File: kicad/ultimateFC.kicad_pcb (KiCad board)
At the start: 8 copper layers, 30.4 x 25.2 mm, 194 parts, among them J1 USB_B_Micro, J2 10132797-011100LF, J3 10132797-011100LF, J4 10132797-011100LF, J5 10132797-011100LF, J6 10132797-011100LF, Q1 DMP2066LSN-7, U1 EFM8BB21F16G-C-QFN20R, U10 NCP81253MNTBG, U11 SiZ200DT, U12 NCP81253MNTBG, U13 SiZ200DT, U14 TPS62824ADMQ, U15 SiZ200DT, U16 NCP81253MNTBG, U17 NCP81253MNTBG, U18 NCP81253MNTBG, U19 NCP81253MNTBG, U2 EFM8BB21F16G-C-QFN20R, U20 SiZ200DT, U21 SiZ200DT, U22 SiZ200DT, U23 SiZ200DT, U24 EFM8BB21F16G-C-QFN20R, U25 NCP81253MNTBG, U26 SiZ200DT, U27 NCP81253MNTBG, U28 NCP81253MNTBG, U29 SiZ200DT, U3 NCP81253MNTBG, U30 SiZ200DT, U31 INA186, U32 LMR33630CQRNX, U33 STM32F745VGHx, U34 AB7456, U35 ZOE-M8Q_ZOE-M8Q, U36 ICM-20602, U37 S25FL064L, U39 BMP280, U4 SiZ200DT, U6 EFM8BB21F16G-C-QFN20R, U7 NCP81253MNTBG, U8 SiZ200DT, U9 NCP81253MNTBG, X1 Molex_734120110, Y1 CSTNE8M00G550000R0, Y2 ECS-270-8-47Q-CES-TR

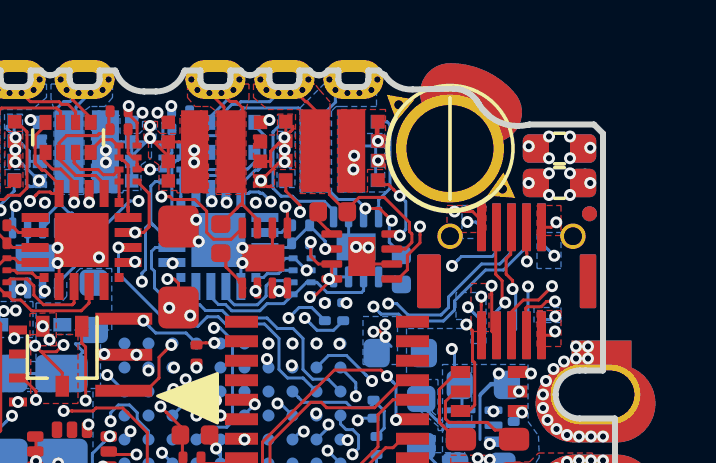
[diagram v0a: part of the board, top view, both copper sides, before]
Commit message: added a few 3d components
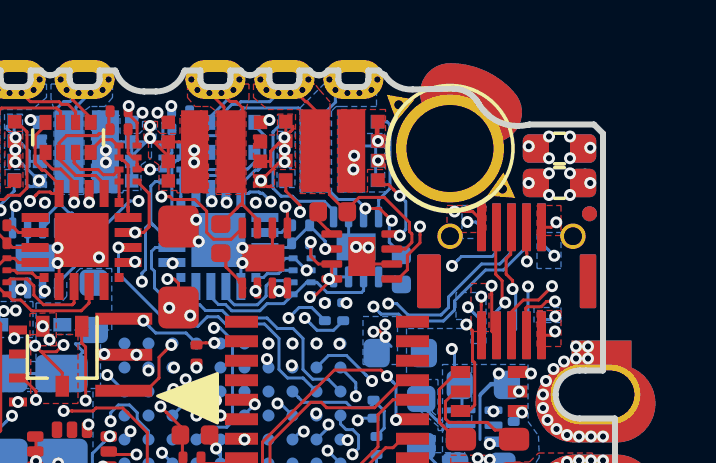
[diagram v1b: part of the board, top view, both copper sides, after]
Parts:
- removed the REF** at (197.1, 64.2) (x2)
- added REF**: Fiducial_0.5mm_Dia_1mm_Outer, Fiducial:Fiducial_0.5mm_Dia_1mm_Outer, F.Cu at (197.1, 64.2)
- added REF**: Fiducial_0.5mm_Dia_1mm_Outer, Fiducial:Fiducial_0.5mm_Dia_1mm_Outer, B.Cu at (197.1, 64.2)
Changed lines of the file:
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@@
   (general
     (thickness 1.2)
-    (drawings 529)
+    (drawings 528)
     (tracks 3920)
     (zones 0)
@@
     (pad 2 smd rect (at 0.6 0.25 90) (size 0.5 0.3) (layers F.Cu F.Paste F.Mask)
       (net 1 GND))
+    (model C:/Users/Christian/Desktop/Elektronik/yolo_fc/yolo-fc/kicad/3D/idc.stp
+      (offset (xyz 0.1 0 0))
+      (scale (xyz 1 1 1))
+      (rotate (xyz -90 0 0))
+    )
   )
   (module ultimateFC:C_AVX_Super_Low_ESL (layer F.Cu)
@@
     (pad 2 smd rect (at 0.6 0.25 90) (size 0.5 0.3) (layers F.Cu F.Paste F.Mask)
       (net 1 GND))
+    (model C:/Users/Christian/Desktop/Elektronik/yolo_fc/yolo-fc/kicad/3D/idc.stp
+      (offset (xyz 0.1 0 0))
+      (scale (xyz 1 1 1))
+      (rotate (xyz -90 0 0))
+    )
   )
   (module ultimateFC:C_AVX_Super_Low_ESL (layer F.Cu)
@@
     (pad 2 smd rect (at 0.6 0.25 90) (size 0.5 0.3) (layers F.Cu F.Paste F.Mask)
       (net 3 +3V3))
+    (model C:/Users/Christian/Desktop/Elektronik/yolo_fc/yolo-fc/kicad/3D/idc.stp
+      (offset (xyz 0.1 0 0))
+      (scale (xyz 1 1 1))
+      (rotate (xyz -90 0 0))
+    )
   )
   (module ultimateFC:C_AVX_Super_Low_ESL (layer B.Cu)
@@
     (pad 2 smd rect (at 0.6 -0.25 270) (size 0.5 0.3) (layers B.Cu B.Paste B.Mask)
       (net 2 +5V))
+    (model C:/Users/Christian/Desktop/Elektronik/yolo_fc/yolo-fc/kicad/3D/idc.stp
+      (offset (xyz 0.1 0 0))
+      (scale (xyz 1 1 1))
+      (rotate (xyz -90 0 0))
+    )
   )
   (module ultimateFC:C_AVX_Super_Low_ESL (layer B.Cu)
@@
     (pad 2 smd rect (at 0.6 -0.25 90) (size 0.5 0.3) (layers B.Cu B.Paste B.Mask)
       (net 1 GND))
+    (model ${KIPRJMOD}/3D/idc.stp
+      (offset (xyz 0.1 0 0))
+      (scale (xyz 1 1 1))
+      (rotate (xyz -90 0 0))
+    )
   )
   (module ultimateFC:C_AVX_Super_Low_ESL (layer F.Cu)
@@
     (pad 2 smd rect (at 0.6 0.25 90) (size 0.5 0.3) (layers F.Cu F.Paste F.Mask)
       (net 1 GND))
+    (model C:/Users/Christian/Desktop/Elektronik/yolo_fc/yolo-fc/kicad/3D/idc.stp
+      (offset (xyz 0.1 0 0))
+      (scale (xyz 1 1 1))
+      (rotate (xyz -90 0 0))
+    )
   )
   (module ultimateFC:C_AVX_Super_Low_ESL (layer B.Cu)
@@
     (pad 2 smd rect (at 0.6 -0.25 90) (size 0.5 0.3) (layers B.Cu B.Paste B.Mask)
       (net 3 +3V3))
+    (model C:/Users/Christian/Desktop/Elektronik/yolo_fc/yolo-fc/kicad/3D/idc.stp
+      (offset (xyz 0.1 0 0))
+      (scale (xyz 1 1 1))
+      (rotate (xyz -90 0 0))
+    )
   )
   (module ultimateFC:C_AVX_Super_Low_ESL (layer B.Cu)
@@
     (pad 2 smd rect (at 0.6 -0.25 270) (size 0.5 0.3) (layers B.Cu B.Paste B.Mask)
       (net 2 +5V))
+    (model C:/Users/Christian/Desktop/Elektronik/yolo_fc/yolo-fc/kicad/3D/idc.stp
+      (offset (xyz 0.1 0 0))
+      (scale (xyz 1 1 1))
+      (rotate (xyz -90 0 0))
+    )
   )
   (module ultimateFC:10132797-011100LF (layer F.Cu)
@@
     (pad 1 smd roundrect (at 1 -1.8 180) (size 0.3 1.6) (layers F.Cu F.Paste F.Mask) (roundrect_rratio 0.1)
       (net 1 GND))
-    (model ${KIPRJMOD}/10132797-011100LF.stp
+    (model ${KIPRJMOD}/3D/10132797-011100LF.stp
       (at (xyz 0 0 0))
       (scale (xyz 1 1 1))
@@
     (pad "" smd roundrect (at 2.75 0 180) (size 0.8 1.8) (layers F.Cu F.Paste F.Mask) (roundrect_rratio 0.1))
     (pad "" smd roundrect (at -2.6 0) (size 0.55 1.8) (layers F.Cu F.Paste F.Mask) (roundrect_rratio 0.1))
-    (model ${KIPRJMOD}/10132797-011100LF.stp
+    (model ${KIPRJMOD}/3D/10132797-011100LF.stp
       (at (xyz 0 0 0))
       (scale (xyz 1 1 1))
@@
     (pad 1 thru_hole circle (at -2.05 -1.5) (size 0.85 0.85) (drill 0.6) (layers *.Cu *.Mask)
       (net 1 GND) (solder_mask_margin -0.05))
-    (model ${KIPRJMOD}/10132797-011100LF.stp
+    (model ${KIPRJMOD}/3D/10132797-011100LF.stp
       (at (xyz 0 0 0))
       (scale (xyz 1 1 1))
@@
   (gr_poly (pts (xy 183.2 67.825) (xy 181.2 67.075) (xy 183.2 66.175)) (layer B.SilkS) (width 0.1))
   (gr_poly (pts (xy 184.75 69.5) (xy 182.75 70.25) (xy 184.75 71.15)) (layer F.SilkS) (width 0.1))
-  (gr_line (start 192.5 60.3) (end 192.5 63.7) (layer F.SilkS) (width 0.12))
   (gr_line (start 196.82 69.4) (end 197.02 69.4) (layer Edge.Cuts) (width 0.2))
   (gr_line (start 197.02 69.4) (end 197.6 69.4) (layer Edge.Cuts) (width 0.2))

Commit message: add drill/placement origin add assembly_output/*.pos
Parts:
- removed the REF** at (197.1, 64.2) (x2)
- added REF**: Fiducial_0.5mm_Dia_1mm_Outer, Fiducial:Fiducial_0.5mm_Dia_1mm_Outer, F.Cu at (197.1, 64.2)
- added REF**: Fiducial_0.5mm_Dia_1mm_Outer, Fiducial:Fiducial_0.5mm_Dia_1mm_Outer, B.Cu at (197.1, 64.2)

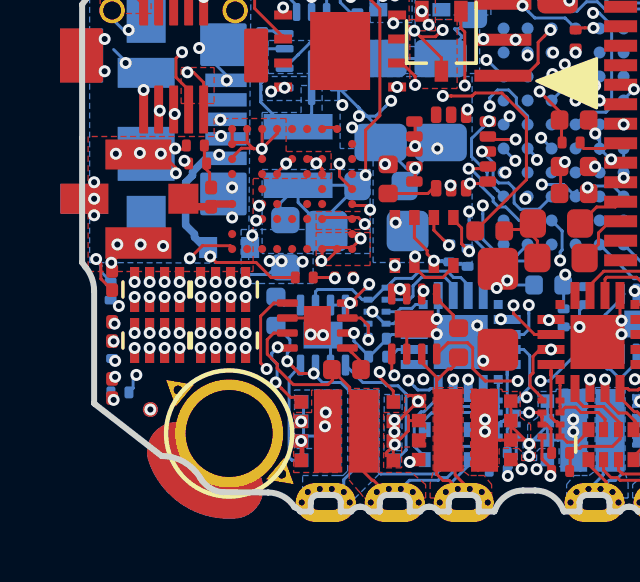
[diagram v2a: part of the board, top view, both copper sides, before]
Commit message: fix footprints (surface mount flag) fix IDC centers update assembly_out/*.pos
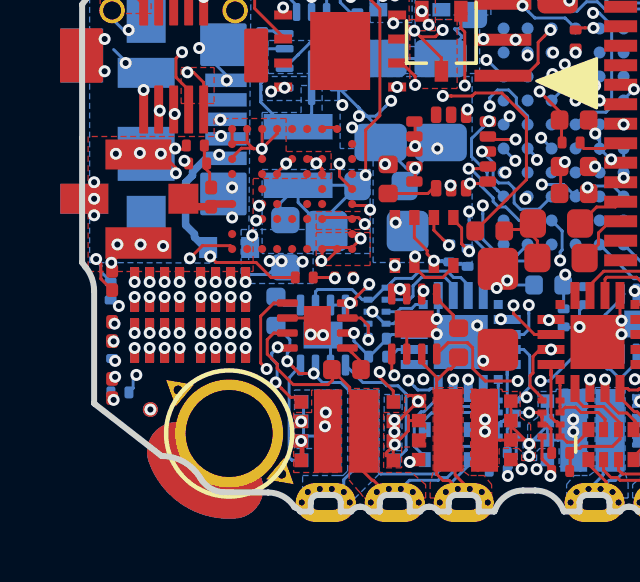
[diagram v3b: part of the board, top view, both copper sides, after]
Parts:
- removed the REF** at (197.1, 64.2) (x2)
- added REF**: Fiducial_0.5mm_Dia_1mm_Outer, Fiducial:Fiducial_0.5mm_Dia_1mm_Outer, F.Cu at (197.1, 64.2)
- added REF**: Fiducial_0.5mm_Dia_1mm_Outer, Fiducial:Fiducial_0.5mm_Dia_1mm_Outer, B.Cu at (197.1, 64.2)
- C14, C15, C20, C21, C41, C42, C43, C44: footprint ultimateFC:C_AVX_Super_Low_ESL -> ultimateFC:C_AVX_Super_Low_ESL_mod
- moved C14 0.10 mm to (172.3, 78.9)
- moved C41 0.10 mm to (172.3, 77.2)
- moved C15 0.10 mm to (170.1, 78.9)
- moved C20 0.10 mm to (172.3, 78.9)
- moved C21 0.10 mm to (170.1, 77.2)
- moved C42 0.10 mm to (170.1, 77.2)
- moved C43 0.10 mm to (172.3, 77.2)
- moved C44 0.10 mm to (170.1, 78.9)

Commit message: fix IDC routing, add fiducials to pos file
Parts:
- removed the REF** at (197.1, 64.2) (x2)
- added REF**: Fiducial_0.5mm_Dia_1mm_Outer, Fiducial:Fiducial_0.5mm_Dia_1mm_Outer, F.Cu at (197.1, 64.2)
- added REF**: Fiducial_0.5mm_Dia_1mm_Outer, Fiducial:Fiducial_0.5mm_Dia_1mm_Outer, B.Cu at (197.1, 64.2)
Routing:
- net GND: track 143.1 -> 151.1 mm
- net +5V: track 36.7 -> 40.7 mm
- net +3V3: track 28.3 -> 32.3 mm
